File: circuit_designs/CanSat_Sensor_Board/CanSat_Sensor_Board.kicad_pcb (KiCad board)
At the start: 4 copper layers, 100 x 100 mm, 25 parts

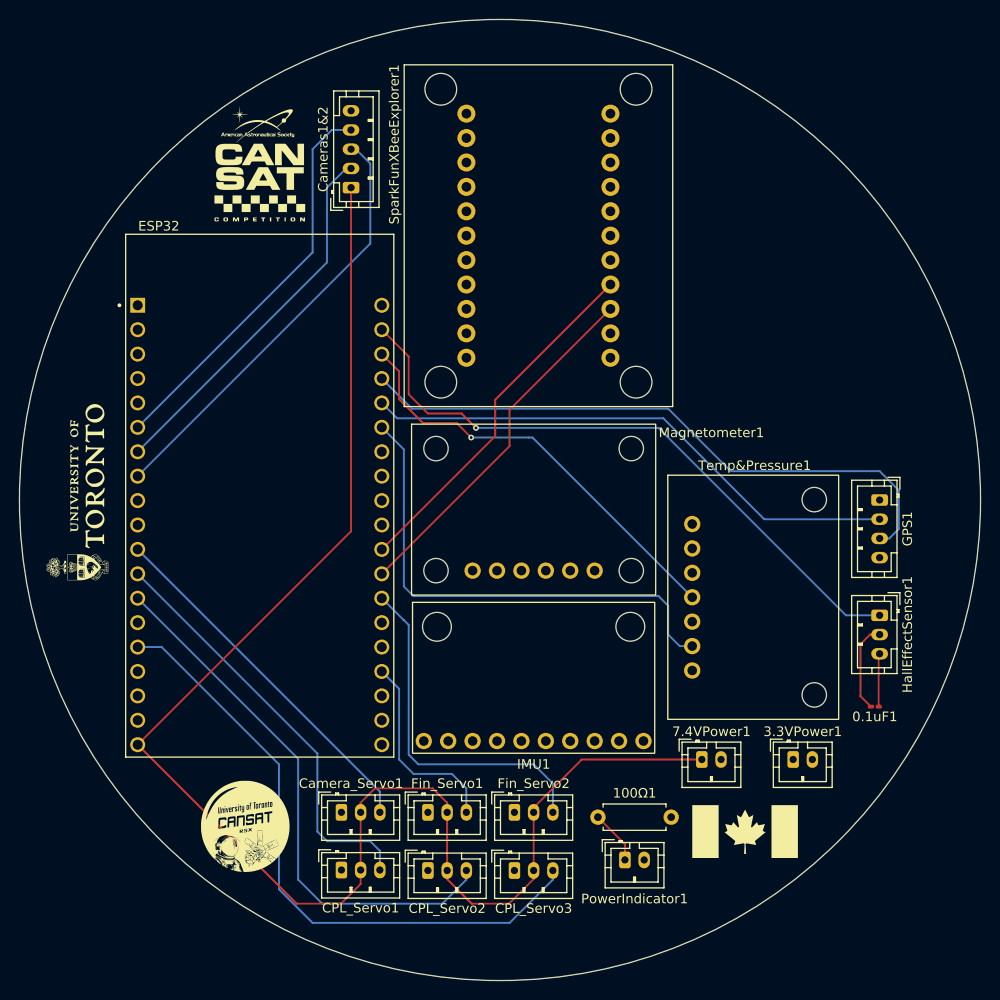
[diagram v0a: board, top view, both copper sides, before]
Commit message: Adding all files including the schematics, layouts, and gerbers for the CanSat sensor and camera boards.
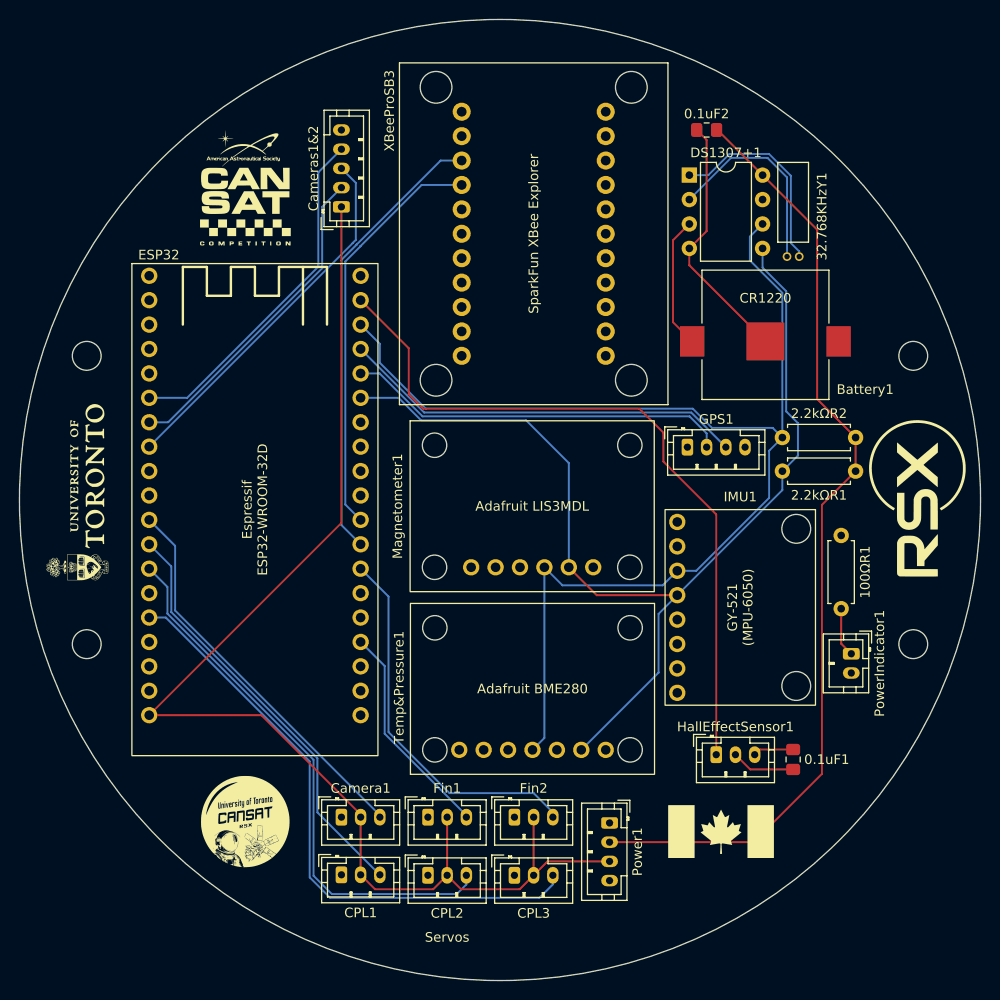
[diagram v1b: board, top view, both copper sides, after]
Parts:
- removed 3.3VPower1, 7.4VPower1: Conn_01x02_Pin, Connector_JST:JST_PH_B2B-PH-K_1x02_P2.00mm_Vertical
- added 0.1uF2: C2, Capacitor_SMD:C_0805_2012Metric_Pad1.18x1.45mm_HandSolder, F.Cu at (171.5, 61.5)
- added 2.2kΩR1: R2, Resistor_THT:R_Axial_DIN0207_L6.3mm_D2.5mm_P7.62mm_Horizontal, F.Cu at (187.0, 97.0)
- added 2.2kΩR2: R3, Resistor_THT:R_Axial_DIN0207_L6.3mm_D2.5mm_P7.62mm_Horizontal, F.Cu at (187.0, 93.5)
- added 32.768KHzY1: AB38T-32.768KHZ, DigiKey:XTAL_AB38T-32.768KHZ, F.Cu at (180.5, 74.7)
- added Battery1: 2894TR, DigiKey:BAT_2894TR, F.Cu at (177.6, 83.5)
- added DS1307+1: DS1307+, Package_DIP:DIP-8_W7.62mm, F.Cu at (169.7, 66.2)
- added G***: LOGO, Graphics:rsx_cansat_logo, F.Cu at (123.5, 133.5)
- added G***: LOGO, Graphics:capybara_astronaut, B.Cu at (177.6, 83.5)
- added Power1: Conn_01x04_Pin, Connector_JST:JST_PH_B4B-PH-K_1x04_P2.00mm_Vertical, F.Cu at (161.4, 133.6)
- 0.1uF1: value C -> C1; footprint Capacitor_SMD:C_0201_0603Metric_Pad0.64x0.40mm_HandSolder -> Capacitor_SMD:C_0805_2012Metric_Pad1.18x1.45mm_HandSolder
- 100ΩR1: renamed from 100Ω1; value R -> R1
- ESP32: footprint ESP32-DEVKITC-32D:MODULE_ESP32-DEVKITC-32D -> Custom_Footprints:ESP32-WROOM-32D_Dev_Board
- IMU1: value GY-BNO08x_(BNO085) -> GY-521_(MPU-6050); footprint Custom_Footprints:GY-BNO08x_(BNO085) -> Custom_Footprints:GY-521_(MPU-6050)
- XBeeProSB3: renamed from SparkFunXBeeExplorer1; value WRL-11812 -> SparkFunXBeeExplorer1
- moved G*** 77.8 mm to (193.5, 100.0), turned to 90 degrees
- moved IMU1 43.0 mm to (182.8, 101.0), turned to -90 degrees
- moved Temp&Pressure1 41.1 mm to (140.7, 128.5), turned to 90 degrees
- moved PowerIndicator1 31.9 mm to (186.6, 116.0), turned to -90 degrees
- moved 100ΩR1 28.0 mm to (185.5, 111.3), turned to 90 degrees
- moved ESP32 27.5 mm to (111.7, 75.4)
- moved HallEffectSensor1 22.3 mm to (172.5, 126.5), turned to 0 degrees
- moved GPS1 20.7 mm to (169.5, 94.5), turned to 0 degrees
- moved 0.1uF1 10.1 mm to (180.5, 127.0), turned to -90 degrees
- moved G*** 2.92 mm to (123.5, 67.5)
- moved G*** 2.50 mm to (173.0, 134.5)
- moved Cameras1&2 2.24 mm to (133.5, 69.5)
- moved G*** 1.58 mm to (124.5, 77.5)
- moved XBeeProSB3 0.53 mm to (153.5, 72.3), turned to 180 degrees
- moved CPL1 0.50 mm to (133.5, 139.0)
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- renumbered CPL_Servo1 to CPL1, CPL_Servo2 to CPL2, CPL_Servo3 to CPL3, Camera_Servo1 to Camera1, Fin_Servo1 to Fin1, Fin_Servo2 to Fin2
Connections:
- net Net-(7.4VPower1-Pin_1) renamed +7.4V
- 0.1uF1 pad 1: Net-(3.3VPower1-Pin_1) -> +3.3V
- 100ΩR1 pad 1: Net-(3.3VPower1-Pin_1) -> Net-(PowerIndicator1-Pin_1)
- 100ΩR1 pad 2: Net-(PowerIndicator1-Pin_1) -> +3.3V
- ESP32 pad J3-3: Net-(ESP32-IO22) -> Net-(DS1307+1-SCL)
- ESP32 pad J3-6: Net-(ESP32-IO21) -> Net-(DS1307+1-SDA)
- GPS1 pad 4: Net-(3.3VPower1-Pin_1) -> +3.3V
- HallEffectSensor1 pad 3: Net-(3.3VPower1-Pin_1) -> +3.3V
- IMU1 pad 1: unconnected-(IMU1-Pin_1-Pad1) -> +3.3V
- IMU1 pad 3: unconnected-(IMU1-Pin_3-Pad3) -> Net-(DS1307+1-SCL)
- IMU1 pad 4: unconnected-(IMU1-Pin_4-Pad4) -> Net-(DS1307+1-SDA)
- Magnetometer1 pad 1: unconnected-(Magnetometer1-Pin_1-Pad1) -> +3.3V
- Magnetometer1 pad 4: unconnected-(Magnetometer1-Pin_4-Pad4) -> Net-(DS1307+1-SCL)
- Magnetometer1 pad 5: unconnected-(Magnetometer1-Pin_5-Pad5) -> Net-(DS1307+1-SDA)
- Temp&Pressure1 pad 1: Net-(3.3VPower1-Pin_1) -> +3.3V
- Temp&Pressure1 pad 4: Net-(ESP32-IO22) -> Net-(DS1307+1-SCL)
- Temp&Pressure1 pad 6: Net-(ESP32-IO21) -> Net-(DS1307+1-SDA)
- XBeeProSB3 pad JP5_10: Net-(3.3VPower1-Pin_1) -> +3.3V
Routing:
- net Net-(DS1307+1-SCL): track 0.00 -> 128.9 mm
- net Net-(DS1307+1-SDA): track 0.00 -> 111.1 mm
- net +5V: track 0.00 -> 99.6 mm
- net Net-(ESP32-IO21): track 51.8 -> 0.00 mm
- net Net-(ESP32-IO22): track 44.5 -> 0.00 mm, vias 1 -> 0
- net +7.4V: track 162.3 -> 134.6 mm
- net GND: track 9.37 -> 33.1 mm
- net Net-(ESP32-TXD0): track 65.0 -> 42.2 mm
- net Net-(DS1307+1-X1): track 0.00 -> 21.2 mm
- net Net-(DS1307+1-X2): track 0.00 -> 21.0 mm
- net Net-(ESP32-RXD0): track 57.3 -> 40.0 mm
- net Net-(DS1307+1-VBAT): track 0.00 -> 13.8 mm
- net Net-(ESP32-IO16): track 37.4 -> 47.2 mm
- net Net-(ESP32-IO23): track 66.4 -> 75.8 mm, vias 1 -> 0
- net Net-(Cameras1&2-Pin_3): track 45.2 -> 38.5 mm
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- added copper zone on In1.Cu, net +3.3V
- removed copper zone on In1.Cu, net Net-(3.3VPower1-Pin_1)
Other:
- outline, holes or cut-outs redrawn
- board text added: "100Ω"
- board text added: "2.2kΩ"
- board text added: "3.3V"
- board text added: "32.768KHz"
- board text added: "3V3"
- board text added: "5V"
- board text added: "7.4V"
- board text added: "ADO"
- board text added: "Adafruit BME280"
- board text added: "Adafruit LIS3MDL"
- board text added: "CR1220"
- board text added: "CTS"
- board text added: "Cam1"
- board text added: "Cam2"
- board text added: "DIN"
- board text added: "DIO0"
- board text added: "DIO1"
- board text added: "DIO11"
- board text added: "DIO12"
- board text added: "DIO2"
- board text added: "DIO3"
- board text added: "DIO4"
- board text added: "DIO5"
- board text added: "DIO9"
- board text added: "DOUT"
- board text added: "DTR"
- board text added: "EN"
- board text added: "Espressif ESP32-WROOM-32D"
- board text added: "GY-521 (MPU-6050)"
- board text added: "INT"
- board text added: "IO0"
- board text added: "IO1"
- board text added: "IO10"
- board text added: "IO11"
- board text added: "IO12"
- board text added: "IO13"
- board text added: "IO14"
- board text added: "IO15"
- board text added: "IO16"
- board text added: "IO17"
- board text added: "IO18"
- board text added: "IO19"
- board text added: "IO2"
- board text added: "IO21"
- board text added: "IO22"
- board text added: "IO23"
- board text added: "IO25"
- board text added: "IO26"
- board text added: "IO27"
- board text added: "IO3"
- board text added: "IO32"
- board text added: "IO33"
- board text added: "IO34"
- board text added: "IO35"
- board text added: "IO36"
- board text added: "IO39"
- board text added: "IO4"
- board text added: "IO5"
- board text added: "IO6"
- board text added: "IO7"
- board text added: "IO8"
- board text added: "IO9"
- board text added: "RES"
- board text added: "RSSI"
- board text added: "RST"
- board text added: "RTS"
- board text added: "RX"
- board text added: "SCL"
- board text added: "SDA"
- board text added: "SQW"
- board text added: "Servos"
- board text added: "Signal"
- board text added: "SparkFun XBee Explorer"
- board text added: "TX"
- board text added: "VBAT"
- board text added: "Vout"
- board text added: "X1"
- board text added: "X2"
- board text added: "XCL"
- board text added: "XDA"
- board text removed: "Sig"
